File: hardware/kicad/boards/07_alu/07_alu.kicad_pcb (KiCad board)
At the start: 2 copper layers, 100 x 99.8 mm, 182 parts, among them J10 Conn_01x04_Pin, J11 Conn_01x04_Pin, J12 Conn_01x08_Pin, J15 Conn_01x08_Pin, J16 Conn_01x08_Pin, J17 Conn_01x08_Pin, J5 Conn_01x08_Pin, J6 Conn_01x08_Pin, J7 Conn_01x08_Pin, U1 74AHC541, U16 74ACT151, U2 74HC00, U3 74ACT283, U36 74HC86, U4 74HC688, U40 74LS377, U41 74ACT151, U42 74ACT151, U43 74ACT151, U44 74ACT151, U45 74ACT151, U46 74ACT151, U47 74ACT151, U48 74ACT151, U49 74ACT151, U5 74ACT283, U50 74ACT151, U51 74ACT151, U52 74ACT151, U53 74ACT151, U54 74ACT151, U55 74ACT151, U56 74ACT151, U6 74HC00

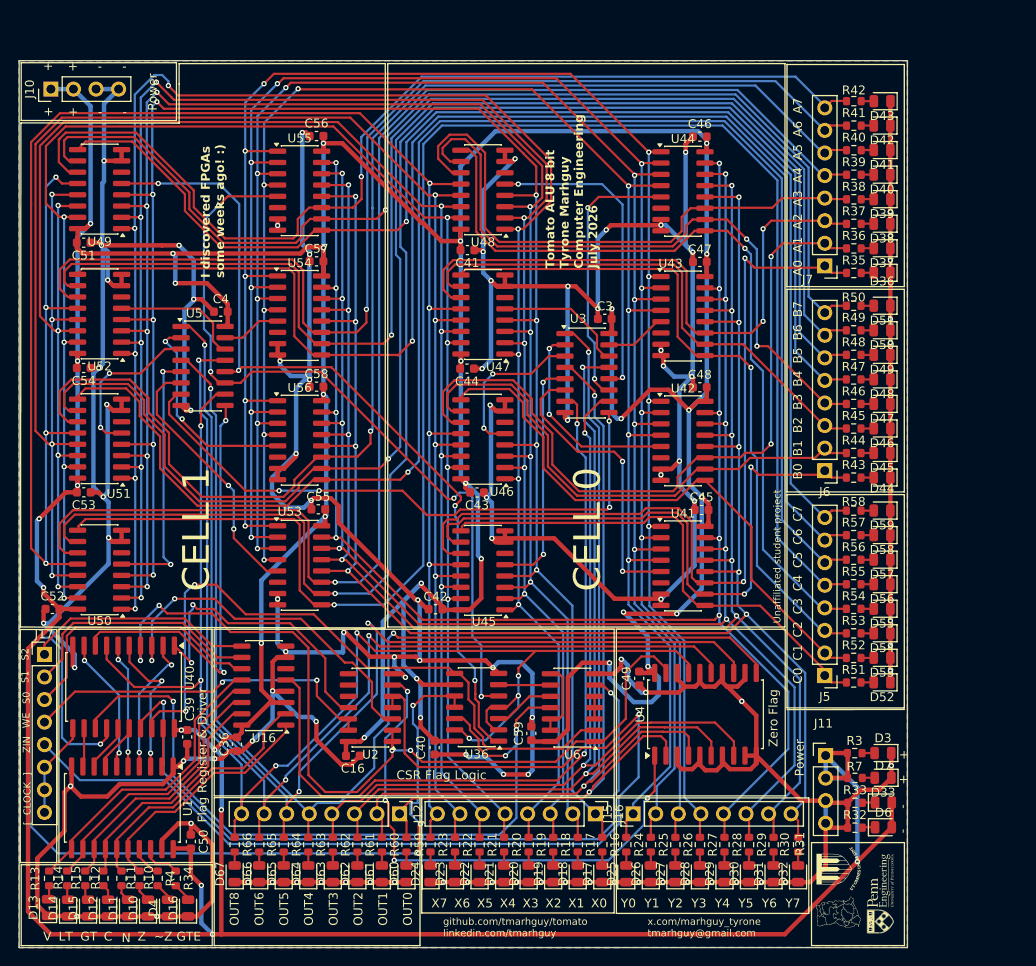
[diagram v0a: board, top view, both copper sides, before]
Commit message: fix: replaced with resistor array/network over individual components
fix #5
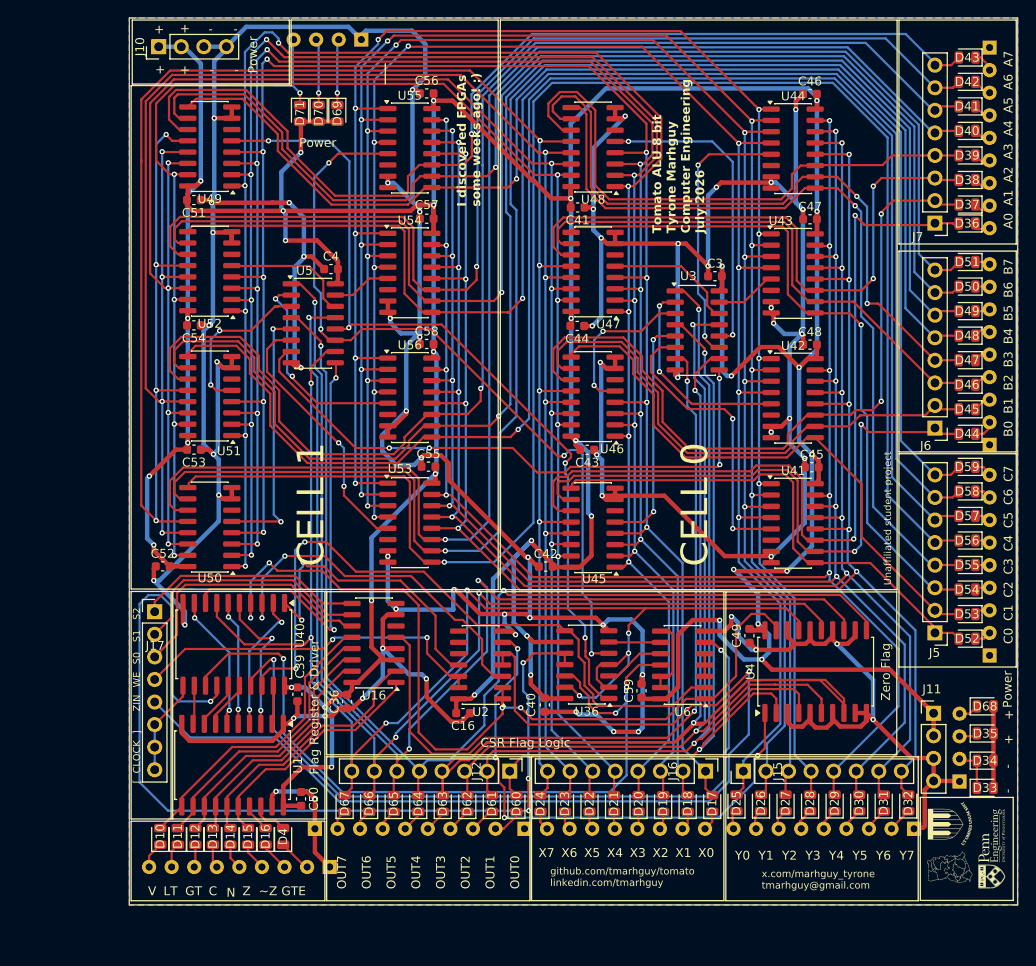
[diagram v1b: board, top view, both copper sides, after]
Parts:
- removed D3, D6, D7: LED, LED_SMD:LED_0805_2012Metric
- removed R10, R11, R12, R13, R14, R15, R16, R17, R18, R19, R20, R21, R22, R23, R24, R25, R26, R27, R28, R29, R30, R31, R34, R35, R36, R37, R38, R39, R4, R40, R41, R42, R43, R44, R45, R46, R47, R48, R49, R50, R51, R52, R53, R54, R55, R56, R57, R58, R59, R60, R61, R62, R63, R64, R65, R66: 330, Resistor_SMD:R_0603_1608Metric
- removed R3, R32, R33, R7: 330 Ohm, Resistor_SMD:R_0603_1608Metric
- added D34: LED, LED_SMD:LED_0805_2012Metric, F.Cu at (171.0, 125.5)
- added D35: LED, LED_SMD:LED_0805_2012Metric, F.Cu at (171.0, 122.5)
- added D68: LED, LED_SMD:LED_0805_2012Metric, F.Cu at (171.0, 119.4)
- added D69: LED, LED_SMD:LED_0805_2012Metric, F.Cu at (98.1, 52.7)
- added D70: LED, LED_SMD:LED_0805_2012Metric, F.Cu at (96.0, 52.7)
- added D71: LED, LED_SMD:LED_0805_2012Metric, F.Cu at (93.9, 52.7)
- added RN1: R_Network08, Resistor_THT:R_Array_SIP9, B.Cu at (163.0, 133.2)
- added RN10: R_Network03, Resistor_THT:R_Array_SIP4, B.Cu at (168.1, 127.9)
- added RN2: R_Network08, Resistor_THT:R_Array_SIP9, B.Cu at (119.2, 133.2)
- added RN3: R_Network08, Resistor_THT:R_Array_SIP9, B.Cu at (95.6, 133.2)
- added RN4: R_Network08, Resistor_THT:R_Array_SIP9, B.Cu at (171.5, 113.7)
- added RN5: R_Network08, Resistor_THT:R_Array_SIP9, B.Cu at (171.5, 90.0)
- added RN6: R_Network08, Resistor_THT:R_Array_SIP9, B.Cu at (171.5, 45.3)
- added RN7: R_Network08, Resistor_THT:R_Array_SIP9, B.Cu at (97.2, 137.5)
- added RN9: R_Network03, Resistor_THT:R_Array_SIP4, B.Cu at (100.8, 44.4)
- U1: value 74AHC541 -> 74ACT541
- U2, U6: value 74HC00 -> 74ACT00
- U36: value 74HC86 -> 74ACT86
- U40: value 74LS377 -> 74ACT377
- moved D13 20.2 mm to (84.1, 134.1)
- moved D14 20.0 mm to (86.1, 134.1)
- moved D15 19.7 mm to (88.1, 134.1)
- moved D4 15.3 mm to (92.0, 134.1)
- moved D26 14.7 mm to (145.8, 130.3)
- moved D27 14.7 mm to (148.5, 130.3)
- moved D28 14.7 mm to (151.3, 130.3)
- moved D30 14.7 mm to (156.8, 130.3)
- moved D31 14.7 mm to (159.6, 130.3)
- moved D32 14.7 mm to (162.3, 130.3)
- moved D25 14.7 mm to (143.0, 130.3)
- moved D29 14.7 mm to (154.1, 130.3)
- moved D17 14.7 mm to (140.3, 130.4)
- moved D21 14.7 mm to (129.2, 130.4)
- moved D64 14.7 mm to (107.2, 130.4)
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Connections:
- D10 pad 1: GND -> Net-(D10-K)
- D10 pad 2: Net-(D10-A) -> flagV
- D11 pad 1: GND -> Net-(D11-K)
- D11 pad 2: Net-(D11-A) -> flagLT
- D12 pad 1: GND -> Net-(D12-K)
- D12 pad 2: Net-(D12-A) -> flagGT
- D13 pad 1: GND -> Net-(D13-K)
- D13 pad 2: Net-(D13-A) -> flagC
- D14 pad 1: GND -> Net-(D14-K)
- D14 pad 2: Net-(D14-A) -> flagN
- D15 pad 1: GND -> Net-(D15-K)
- D15 pad 2: Net-(D15-A) -> flagZ
- D16 pad 1: GND -> Net-(D16-K)
- D16 pad 2: Net-(D16-A) -> ~flagZ
- D17 pad 1: GND -> Net-(D17-K)
- D17 pad 2: Net-(D17-A) -> ALU_OPCODE_X0
- D18 pad 1: GND -> Net-(D18-K)
- D18 pad 2: Net-(D18-A) -> ALU_OPCODE_X1
- D19 pad 1: GND -> Net-(D19-K)
- D19 pad 2: Net-(D19-A) -> ALU_OPCODE_X2
- D20 pad 1: GND -> Net-(D20-K)
- D20 pad 2: Net-(D20-A) -> ALU_OPCODE_X3
- D21 pad 1: GND -> Net-(D21-K)
- D21 pad 2: Net-(D21-A) -> ALU_OPCODE_X4
- D22 pad 1: GND -> Net-(D22-K)
- D22 pad 2: Net-(D22-A) -> ALU_OPCODE_X5
- D23 pad 1: GND -> Net-(D23-K)
- D23 pad 2: Net-(D23-A) -> ALU_OPCODE_X6
- D24 pad 1: GND -> Net-(D24-K)
- D24 pad 2: Net-(D24-A) -> ALU_OPCODE_X7
- D25 pad 1: GND -> Net-(D25-K)
- D25 pad 2: Net-(D25-A) -> ALU_OPCODE_Y0
- D26 pad 1: GND -> Net-(D26-K)
- D26 pad 2: Net-(D26-A) -> ALU_OPCODE_Y1
- D27 pad 1: GND -> Net-(D27-K)
- D27 pad 2: Net-(D27-A) -> ALU_OPCODE_Y2
- D28 pad 1: GND -> Net-(D28-K)
- D28 pad 2: Net-(D28-A) -> ALU_OPCODE_Y3
- D29 pad 1: GND -> Net-(D29-K)
- D29 pad 2: Net-(D29-A) -> ALU_OPCODE_Y4
- D30 pad 1: GND -> Net-(D30-K)
- D30 pad 2: Net-(D30-A) -> ALU_OPCODE_Y5
- D31 pad 1: GND -> Net-(D31-K)
- D31 pad 2: Net-(D31-A) -> ALU_OPCODE_Y6
- D32 pad 1: GND -> Net-(D32-K)
- D32 pad 2: Net-(D32-A) -> ALU_OPCODE_Y7
- D33 pad 1: GND -> Net-(D33-K)
- D33 pad 2: Net-(D33-A) -> VCC
- D36 pad 1: GND -> Net-(D36-K)
- D36 pad 2: Net-(D36-A) -> A0
- D37 pad 1: GND -> Net-(D37-K)
- D37 pad 2: Net-(D37-A) -> A1
- D38 pad 1: GND -> Net-(D38-K)
- D38 pad 2: Net-(D38-A) -> A2
- D39 pad 1: GND -> Net-(D39-K)
- D39 pad 2: Net-(D39-A) -> A3
- D4 pad 1: GND -> Net-(D4-K)
- D4 pad 2: Net-(D4-A) -> flagGTE
- D40 pad 1: GND -> Net-(D40-K)
- D40 pad 2: Net-(D40-A) -> A4
- D41 pad 1: GND -> Net-(D41-K)
- D41 pad 2: Net-(D41-A) -> A5
- D42 pad 1: GND -> Net-(D42-K)
- D42 pad 2: Net-(D42-A) -> A6
- D43 pad 1: GND -> Net-(D43-K)
- D43 pad 2: Net-(D43-A) -> A7
- D44 pad 1: GND -> Net-(D44-K)
- D44 pad 2: Net-(D44-A) -> B0
- D45 pad 1: GND -> Net-(D45-K)
- D45 pad 2: Net-(D45-A) -> B1
- D46 pad 1: GND -> Net-(D46-K)
- D46 pad 2: Net-(D46-A) -> B2
- D47 pad 1: GND -> Net-(D47-K)
- D47 pad 2: Net-(D47-A) -> B3
- D48 pad 1: GND -> Net-(D48-K)
- D48 pad 2: Net-(D48-A) -> B4
- D49 pad 1: GND -> Net-(D49-K)
- D49 pad 2: Net-(D49-A) -> B5
- D50 pad 1: GND -> Net-(D50-K)
- D50 pad 2: Net-(D50-A) -> B6
- D51 pad 1: GND -> Net-(D51-K)
- D51 pad 2: Net-(D51-A) -> B7
- D52 pad 1: GND -> Net-(D52-K)
- D52 pad 2: Net-(D52-A) -> C0
- D53 pad 1: GND -> Net-(D53-K)
- D53 pad 2: Net-(D53-A) -> C1
- D54 pad 1: GND -> Net-(D54-K)
- D54 pad 2: Net-(D54-A) -> C2
- D55 pad 1: GND -> Net-(D55-K)
- D55 pad 2: Net-(D55-A) -> C3
- D56 pad 1: GND -> Net-(D56-K)
- D56 pad 2: Net-(D56-A) -> C4
- D57 pad 1: GND -> Net-(D57-K)
- D57 pad 2: Net-(D57-A) -> C5
- D58 pad 1: GND -> Net-(D58-K)
- D58 pad 2: Net-(D58-A) -> C6
- D59 pad 1: GND -> Net-(D59-K)
- D59 pad 2: Net-(D59-A) -> C7
- D60 pad 1: GND -> Net-(D60-K)
- D60 pad 2: Net-(D60-A) -> OUT0
- D61 pad 1: GND -> Net-(D61-K)
- D61 pad 2: Net-(D61-A) -> OUT1
- D62 pad 1: GND -> Net-(D62-K)
- D62 pad 2: Net-(D62-A) -> OUT2
- D63 pad 1: GND -> Net-(D63-K)
- D63 pad 2: Net-(D63-A) -> OUT3
- D64 pad 1: GND -> Net-(D64-K)
- D64 pad 2: Net-(D64-A) -> OUT4
- D65 pad 1: GND -> Net-(D65-K)
- D65 pad 2: Net-(D65-A) -> OUT5
- D66 pad 1: GND -> Net-(D66-K)
- D66 pad 2: Net-(D66-A) -> OUT6
- D67 pad 1: GND -> Net-(D67-K)
- D67 pad 2: Net-(D67-A) -> OUT7
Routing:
- net GND: track 824.2 -> 681.4 mm, vias 95 -> 63
- net VCC: track 710.4 -> 576.2 mm, vias 36 -> 35
- net OUT3: track 97.7 -> 151.7 mm
- net Net-(D70-K): track 0.00 -> 8.19 mm, vias 0 -> 1
- net Net-(D69-K): track 0.00 -> 8.00 mm, vias 0 -> 1
- net Net-(D71-K): track 0.00 -> 7.74 mm, vias 0 -> 1
- net Net-(D33-K): track 0.00 -> 5.09 mm
- net Net-(D4-K): track 0.00 -> 3.73 mm
- net Net-(D60-K): track 0.00 -> 3.41 mm
- net Net-(D16-K): track 0.00 -> 3.36 mm
- net Net-(D15-K): track 0.00 -> 3.15 mm
- net Net-(D10-K): track 0.00 -> 3.02 mm
- net Net-(D61-K): track 0.00 -> 2.92 mm
- net Net-(D14-K): track 0.00 -> 2.92 mm
- net Net-(D11-K): track 0.00 -> 2.79 mm
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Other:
- board text added: "OUT7"
- board text removed: "OUT8"
